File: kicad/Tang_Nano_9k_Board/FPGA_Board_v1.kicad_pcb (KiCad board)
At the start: 2 copper layers, 100 x 100 mm, 29 parts, among them J1 Conn_01x24, J2 Conn_01x24, J3 Conn_01x08, J4 Conn_01x04, J5 Conn_01x04, J6 Conn_01x04, J7 Conn_01x04, J8 Conn_01x06, SW1 SW_DIP_x08, SW2 SW_Push, SW3 SW_Push, SW4 SW_Push, U3 TBD62786APG, U4 74HC138

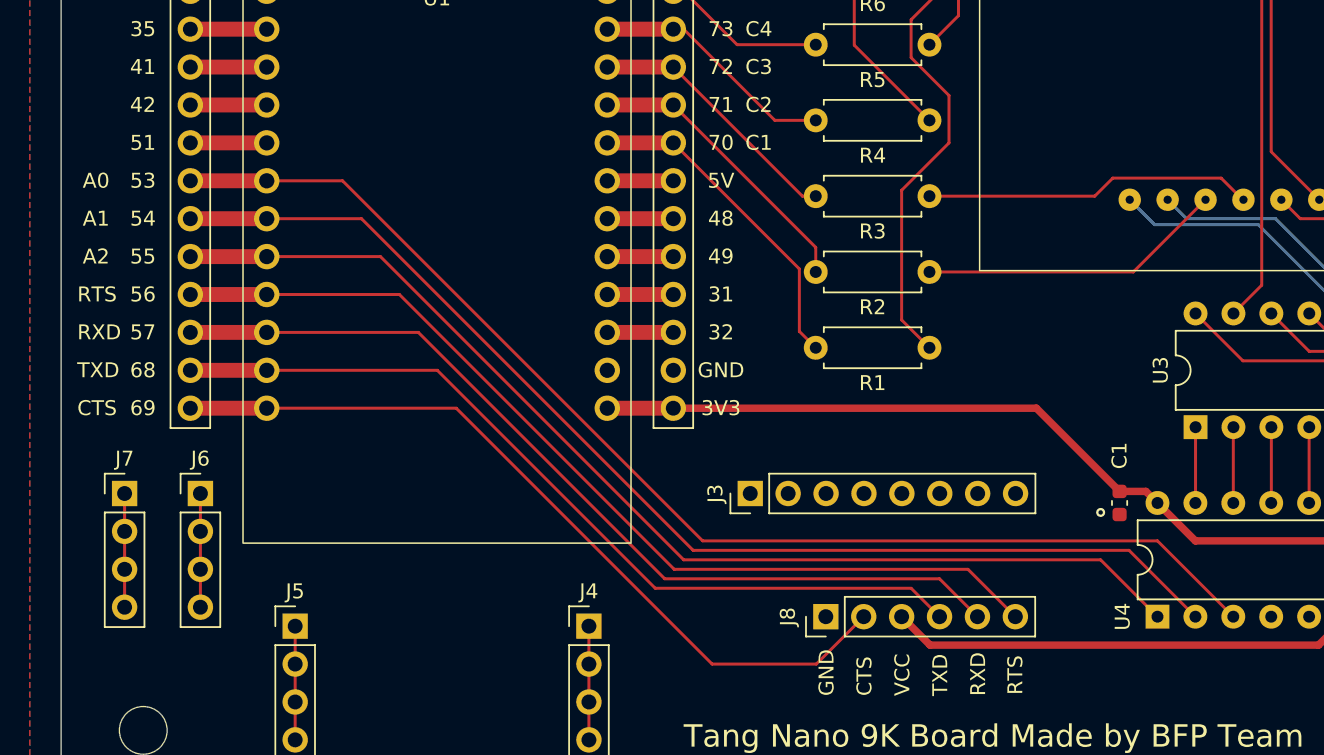
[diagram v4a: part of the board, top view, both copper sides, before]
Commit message: modify shematic, shift the UART pin up
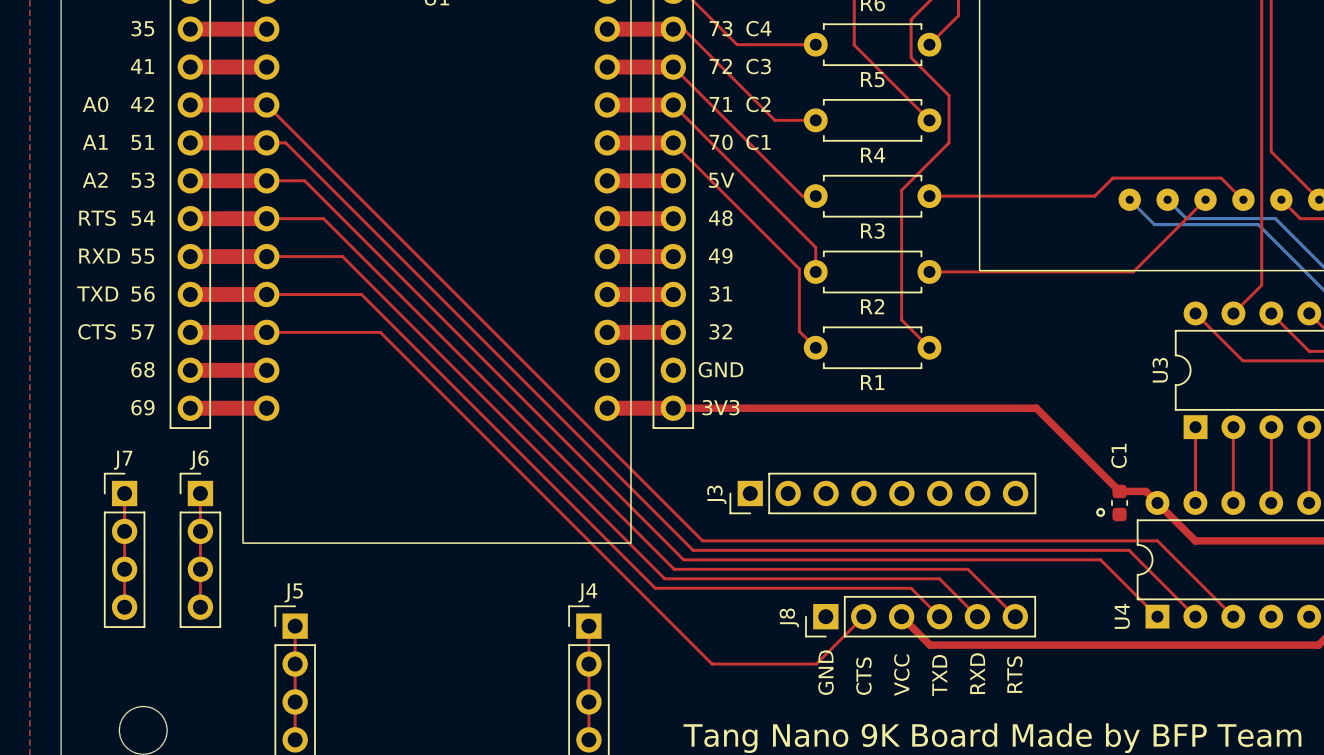
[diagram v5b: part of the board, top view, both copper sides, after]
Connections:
- J1 pad 16: Net-(J1-Pin_16) -> /A2
- J1 pad 17: Net-(J1-Pin_17) -> /A1
- J1 pad 18: /A2 -> /A0
- J1 pad 19: /A1 -> /RTS
- J1 pad 20: /A0 -> /RXD
- J1 pad 21: /RTS -> /TXD
- J1 pad 22: /RXD -> /CTS
- J1 pad 23: /TXD -> Net-(J1-Pin_23)
- J1 pad 24: /CTS -> Net-(J1-Pin_24)
- U1 pad 16: Net-(J1-Pin_16) -> /A2
- U1 pad 17: Net-(J1-Pin_17) -> /A1
- U1 pad 18: /A2 -> /A0
- U1 pad 19: /A1 -> /RTS
- U1 pad 20: /A0 -> /RXD
- U1 pad 21: /RTS -> /TXD
- U1 pad 22: /RXD -> /CTS
- U1 pad 23: /TXD -> Net-(J1-Pin_23)
- U1 pad 24: /CTS -> Net-(J1-Pin_24)
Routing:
- net Net-(J1-Pin_24): track 0.00 -> 5.12 mm
- net Net-(J1-Pin_23): track 0.00 -> 5.12 mm
- net Net-(J1-Pin_17): track 5.12 -> 0.00 mm
- net Net-(J1-Pin_16): track 5.12 -> 0.00 mm
- net /A1: track 78.4 -> 80.5 mm
- net /A0: track 74.8 -> 76.9 mm
- net /TXD: track 57.0 -> 59.1 mm
- net /CTS: track 53.5 -> 55.6 mm
- net /RXD: track 60.6 -> 62.7 mm
- net /RTS: track 64.2 -> 66.3 mm
- net /A2: track 82.0 -> 84.1 mm
